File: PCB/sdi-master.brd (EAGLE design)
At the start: 71 x 18.6 mm, 21 parts, among them J3 1X2-3.5MM, J4 POWER_JACKPTH_LOCK, U1 ATSAMD11C14A-SSUT, U3 LDL1117S12R

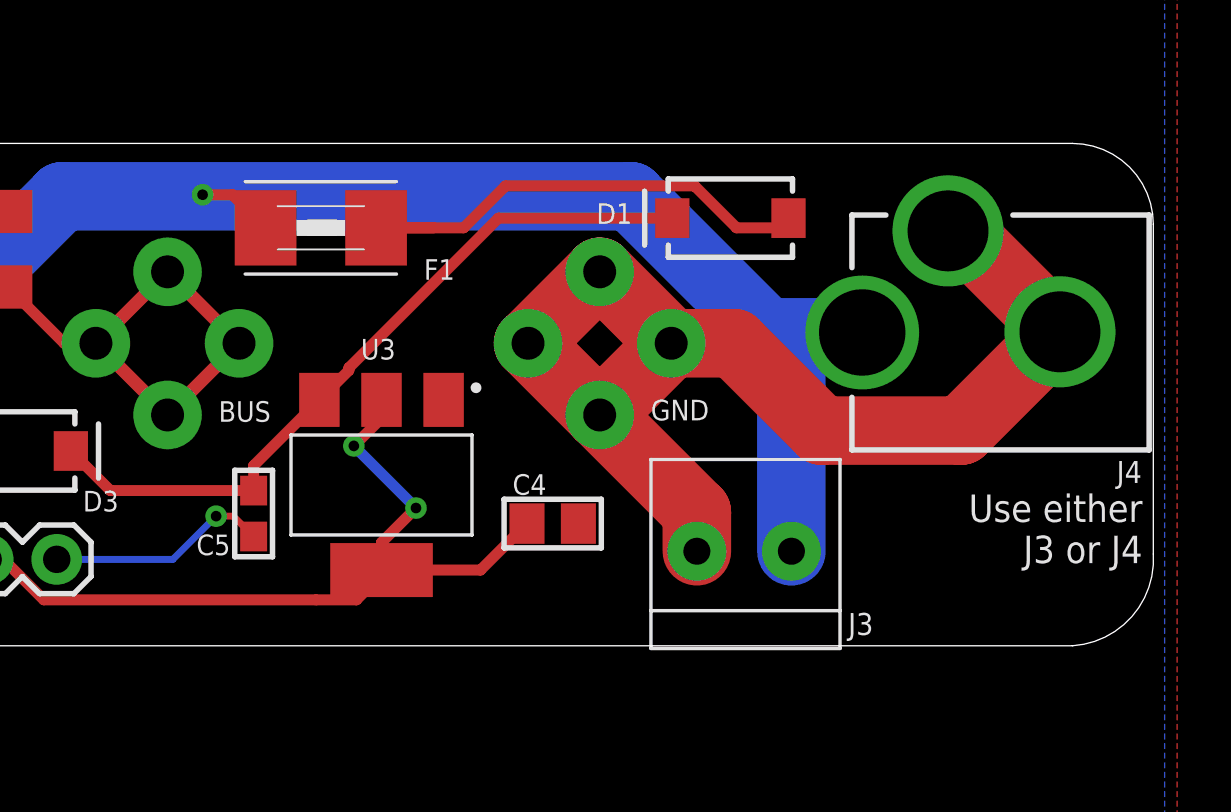
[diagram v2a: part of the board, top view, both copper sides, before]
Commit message: replaced 2 position terminal with 3 positions
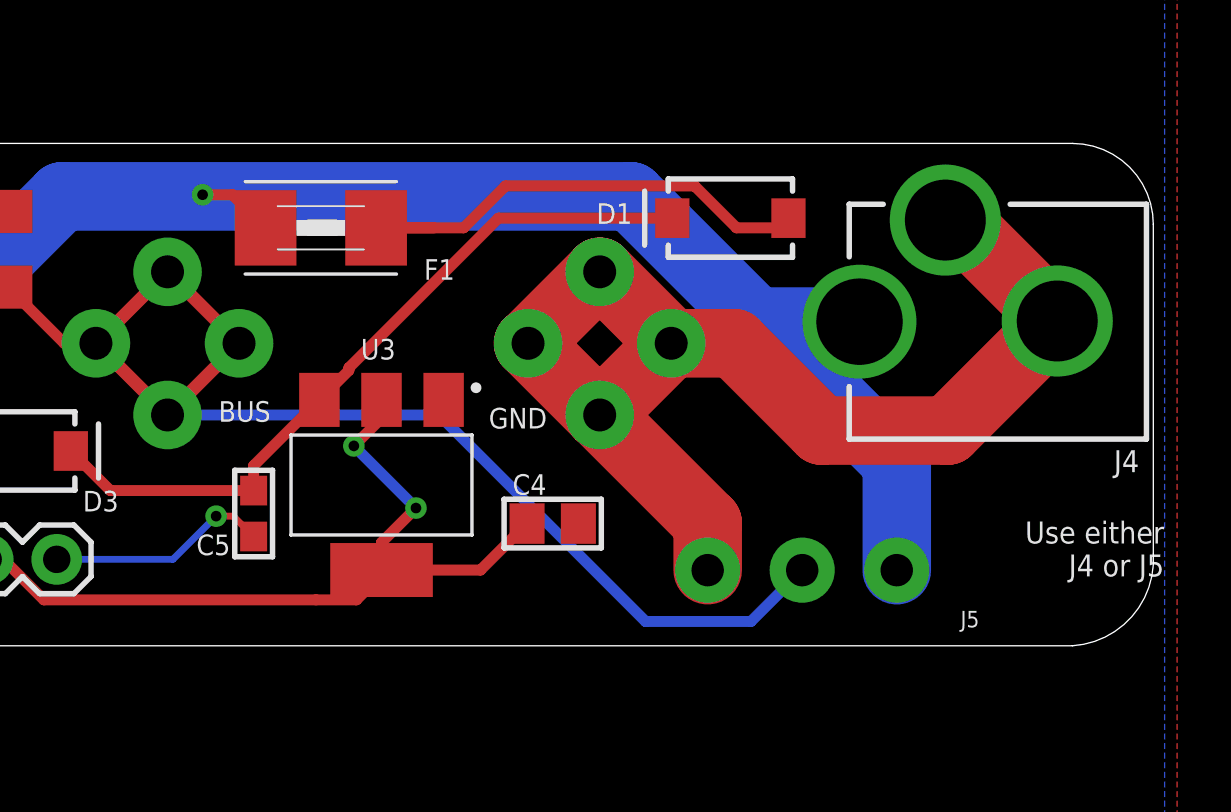
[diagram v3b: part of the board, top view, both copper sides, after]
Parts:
- removed J3: 1X2-3.5MM, Adafruit:1X2-3.5MM
- added J5: (no value), SparkFun-Connectors:SCREWTERMINAL-3.5MM-3-NS
- moved J4 0.41 mm to (74.0, 20.8)
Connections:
- net BUS: now also J5.2
- net GND: now also J5.1; no longer J3.2
- net VCC-RAW: now also J5.3; no longer J3.1
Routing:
- net BUS: track 19.3 -> 46.7 mm
- net VCC-RAW: track 77.3 -> 80.0 mm
- net GND: track 52.7 -> 53.7 mm
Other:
- board text added: "GND BUS VCC"
- board text added: "Use either J4 or J5"
- board text removed: "Use either J3 or J4"
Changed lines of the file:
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@@
 <?xml version="1.0" encoding="utf-8"?>
 <!DOCTYPE eagle SYSTEM "eagle.dtd">
-<eagle version="9.2.2">
+<eagle version="9.3.0">
 <drawing>
 <settings>
-<setting alwaysvectorfont="yes"/>
+<setting alwaysvectorfont="no"/>
 <setting keepoldvectorfont="yes"/>
 <setting verticaltext="up"/>
@@
 <fusionsync huburn="a.cGVyc29uYWw6dWUyODAzZDk0" projecturn="a.cGVyc29uYWw6dWUyODAzZDk0IzIwMTgwMzE2MTIzMTg0Mjgx" f3durn="urn:adsk.wipprod:dm.lineage:DvfZjGxoRsOmgfsErQWE_A" pcbguid="6383e179-ef03-4662-8bce-4f58b75482cc" lastpulledtime="" lastsyncedchangeguid="90d3d4ca-2862-99f0-234d-071efe203a04"/>
 <plain>
-<text x="52.394" y="17.1452" size="0.762" layer="25" font="vector" ratio="15">GND</text>
+<text x="46.394" y="16.8452" size="0.762" layer="25" font="vector" ratio="15">GND</text>
 <text x="36.392" y="17.0944" size="0.762" layer="25" font="vector" ratio="15">BUS</text>
 <text x="24.0476" y="17.196" size="0.762" layer="25" font="vector" ratio="15">VCC</text>
@@
 <text x="25.9524" y="17.196" size="0.762" layer="26" font="vector" ratio="15" rot="MR0">VCC</text>
 <text x="38.308" y="17.0944" size="0.762" layer="26" font="vector" ratio="15" rot="MR0">BUS</text>
-<text x="54.406" y="17.1452" size="0.762" layer="26" font="vector" ratio="15" rot="MR0">GND</text>
-<text x="70.6" y="14.4" size="1.016" layer="25" font="vector" rot="R180">Use either
-J3 or J4</text>
+<text x="48.406" y="16.8452" size="0.762" layer="26" font="vector" ratio="15" rot="MR0">GND</text>
+<text x="71.4" y="13.4" size="0.8128" layer="25" font="vector" rot="R180">Use either
+J4 or J5</text>
+<text x="53.7" y="15.2" size="0.8128" layer="255">GND  BUS  VCC</text>
 </plain>
 <attributes>
@@
 <attribute name="VALUE" x="31.67" y="14.032" size="0.6096" layer="27" font="vector" ratio="20" rot="R180"/>
 </element>
-<element name="J3" library="Adafruit" package="1X2-3.5MM" value="1X2-3.5MM" x="55.8" y="12.3" smashed="yes">
-<attribute name="NAME" x="59.7" y="9.2" size="0.8128" layer="25"/>
-</element>
-<element name="J4" library="SparkFun-Connectors" package="POWER_JACK_PTH_LOCK" value="POWER_JACKPTH_LOCK" x="74.1" y="20.4" smashed="yes" rot="R90">
-<attribute name="NAME" x="70.5748" y="15.641" size="0.8128" layer="25" font="vector" ratio="20" rot="R180"/>
-<attribute name="PROD_ID" value="CONN-08197" x="74.1" y="20.4" size="1.778" layer="27" rot="R90" display="off"/>
-<attribute name="SF_ID" value="PRT-00119" x="74.1" y="20.4" size="1.778" layer="27" rot="R90" display="off"/>
-<attribute name="VALUE" x="68.105" y="27.057" size="0.6096" layer="27" font="vector" ratio="20" rot="R180"/>
+<element name="J4" library="SparkFun-Connectors" package="POWER_JACK_PTH_LOCK" value="POWER_JACKPTH_LOCK" x="74" y="20.8" smashed="yes" rot="R90">
+<attribute name="NAME" x="70.4748" y="16.041" size="0.8128" layer="25" font="vector" ratio="20" rot="R180"/>
+<attribute name="PROD_ID" value="CONN-08197" x="74" y="20.8" size="1.778" layer="27" rot="R90" display="off"/>
+<attribute name="SF_ID" value="PRT-00119" x="74" y="20.8" size="1.778" layer="27" rot="R90" display="off"/>
+<attribute name="VALUE" x="84.705" y="22.257" size="0.6096" layer="27" font="vector" ratio="20" rot="R180"/>
+</element>
+<element name="J5" library="SparkFun-Connectors" library_urn="urn:adsk.eagle:library:513" package="SCREWTERMINAL-3.5MM-3-NS" package3d_urn="urn:adsk.eagle:package:38088/1" value="" x="54.5" y="11.6" smashed="yes">
+<attribute name="NAME" x="63.859" y="9.483" size="0.6096" layer="25" font="vector" ratio="20"/>
+<attribute name="VALUE" x="56.532" y="7.028" size="0.6096" layer="27" font="vector" ratio="20"/>
 </element>
 </elements>
@@
 <wire x1="53.15" y1="20" x2="55.485775" y2="20" width="2.54" layer="1"/>
 <wire x1="55.485775" y1="20" x2="58.717775" y2="16.768" width="2.54" layer="1"/>
-<wire x1="58.717775" y1="16.768" x2="63.8856" y2="16.768" width="2.54" layer="1"/>
-<wire x1="63.8856" y1="16.768" x2="67.543" y2="20.4254" width="2.54" layer="1"/>
-<wire x1="50.502" y1="17.346" x2="54.1" y2="13.748" width="2.54" layer="1"/>
-<contactref element="J3" pad="2"/>
-<wire x1="54.1" y1="13.748" x2="54.1" y2="12.3" width="2.54" layer="1"/>
-<wire x1="67.543" y1="20.4254" x2="63.8068" y2="24.1616" width="2.54" layer="1"/>
-<wire x1="63.8068" y1="24.1616" x2="63.4" y2="24.1616" width="2.54" layer="1"/>
-<wire x1="44.724" y1="17.904" x2="47.856" y2="20" width="0" layer="19" extent="1-1"/>
-<wire x1="49.712" y1="13.325" x2="50.502" y2="17.348" width="0" layer="19" extent="1-1"/>
-<wire x1="37.69" y1="12.847" x2="44.724" y2="17.904" width="0" layer="19" extent="1-1"/>
-<wire x1="12.31" y1="18.6452" x2="30.4" y2="12" width="0" layer="19" extent="1-1"/>
-<wire x1="9.2844" y1="21.1468" x2="12.31" y2="18.6452" width="0" layer="19" extent="1-1"/>
-<wire x1="1.957" y1="20.255" x2="9.2844" y2="21.1468" width="0" layer="19" extent="1-1"/>
-<wire x1="1.957" y1="16.57" x2="1.957" y2="20.255" width="0" layer="19" extent="1-1"/>
-<wire x1="4.682" y1="15.27" x2="1.957" y2="16.57" width="0" layer="19" extent="1-1"/>
-<wire x1="1.957" y1="12.885" x2="4.682" y2="15.27" width="0" layer="19" extent="1-1"/>
+<wire x1="58.717775" y1="16.768" x2="63.3856" y2="16.768" width="2.54" layer="1"/>
+<wire x1="63.3856" y1="16.768" x2="67.443" y2="20.8254" width="2.54" layer="1"/>
+<wire x1="50.502" y1="17.346" x2="54.5" y2="13.348" width="2.54" layer="1"/>
+<wire x1="67.443" y1="20.8254" x2="63.7068" y2="24.5616" width="2.54" layer="1"/>
+<wire x1="63.7068" y1="24.5616" x2="63.3" y2="24.5616" width="2.54" layer="1"/>
+<contactref element="J5" pad="1"/>
+<wire x1="54.5" y1="13.348" x2="54.5" y2="11.6" width="2.54" layer="1"/>
 </signal>
 <signal name="PWM">
@@
 <wire x1="36.905" y1="25.5" x2="38.131" y2="24.274" width="0.4064" layer="1"/>
 <contactref element="J4" pad="PWR"/>
-<wire x1="60.2222" y1="20.4" x2="56.70131875" y2="20.4" width="2.54" layer="16"/>
-<wire x1="56.70131875" y1="20.4" x2="51.66131875" y2="25.44" width="2.54" layer="16"/>
+<wire x1="60.1222" y1="20.8" x2="56.30131875" y2="20.8" width="2.54" layer="16"/>
+<wire x1="56.30131875" y1="20.8" x2="51.66131875" y2="25.44" width="2.54" layer="16"/>
 <wire x1="51.66131875" y1="25.44" x2="30.59" y2="25.44" width="2.54" layer="16"/>
 <wire x1="30.59" y1="25.44" x2="25.15" y2="20" width="2.54" layer="16"/>
@@
 <wire x1="22.498" y1="17.344" x2="25.15" y2="19.996" width="2.54" layer="16"/>
 <wire x1="25.15" y1="19.996" x2="25.15" y2="20" width="2.54" layer="16"/>
-<contactref element="J3" pad="1"/>
-<wire x1="56.70131875" y1="20.4" x2="57.6" y2="19.50131875" width="2.54" layer="16"/>
-<wire x1="57.6" y1="19.50131875" x2="57.6" y2="12.3" width="2.54" layer="16"/>
-<wire x1="30.59" y1="25.44" x2="35.8" y2="25.5" width="0" layer="19" extent="1-16"/>
+<contactref element="J5" pad="3"/>
+<wire x1="56.30131875" y1="20.8" x2="61.5" y2="15.60131875" width="2.54" layer="16"/>
+<wire x1="61.5" y1="15.60131875" x2="61.5" y2="11.6" width="2.54" layer="16"/>
 </signal>
 <signal name="USB+">
@@
 <wire x1="28.598" y1="22.08" x2="30.678" y2="20" width="0.4064" layer="1"/>
 <wire x1="30.678" y1="20" x2="31.85" y2="20" width="0.4064" layer="1"/>
+<contactref element="J5" pad="2"/>
+<wire x1="34.502" y1="17.346" x2="44.554" y2="17.346" width="0.4064" layer="16"/>
+<wire x1="56.1" y1="9.7" x2="58" y2="11.6" width="0.4064" layer="16"/>
+<wire x1="44.554" y1="17.346" x2="52.2" y2="9.7" width="0.4064" layer="16"/>
+<wire x1="52.2" y1="9.7" x2="56.1" y2="9.7" width="0.4064" layer="16"/>
 </signal>
 <signal name="N$6">
